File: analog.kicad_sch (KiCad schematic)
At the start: 51 parts, among them J10 Sensor harness, U8 ADS1115

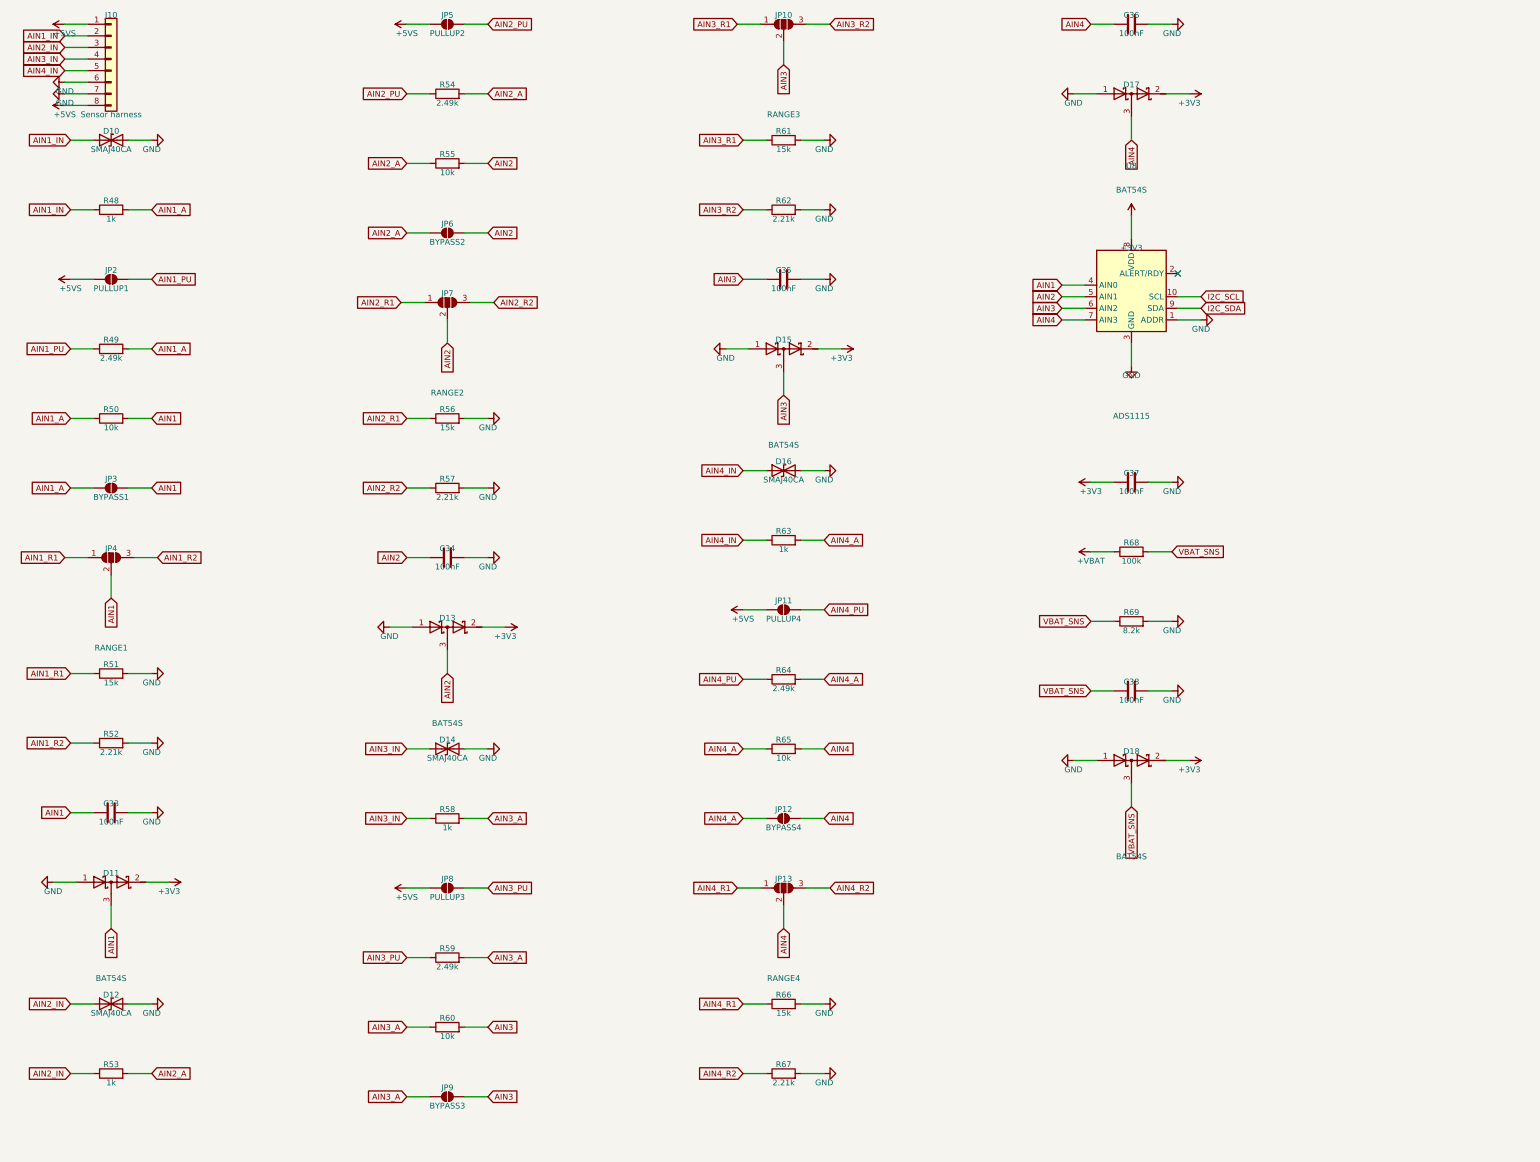
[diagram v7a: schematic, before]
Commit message: Rev B is fully routed: zero DRC errors, nothing unconnected
84 x 84 mm, 1447 tracks, 258 vias, 179 footprints, 106 nets.

The last few connections were never routing problems. Each one was a part
sited away from the net it belongs to, and the autorouter reporting "no
path at any width" was telling the truth:

  +5VS  the sensor rail's source (PF1/FB2/D3) sat on the right beside the
        WS2812 header while everything it feeds -- the sensor harness and
        all four channel pull-ups -- is on the left. The net existed as
        two complete halves with a 45 mm gap through buck islands and the
        SD socket. Moved the source to the harness side.
  IO46  the strapping pull-downs were parked in the bottom band while
        IO3/IO45/IO46 run from the module's south pads to J7 at the top
        left, so R29 needed a trace the length of the board to reach its
        own net. Moved them under the module's south pads.

Adding router passes had never touched either. Moving the parts fixed
both immediately -- worth remembering next time a net "cannot be routed".

Also in this pass:

  - One LED. D6 (amber) and D7 (blue) and their resistors are gone; D4
    green stays on +3V3, which is the right rail to watch because it only
    lights if the whole chain came through -- battery, ideal diode, both
    converters. That also retires review item 11.2.10, the blue emitter
    that would have been near-invisible on a 3.288 V rail.
  - J7 grows to six pins: the three strapping pins, the two GPIOs freed
    by the LEDs (IO15/IO16), and a ground pin. The missing ground was
    review item 13.4.13.
  - USB_CC1 gets a Fine netclass at 0.2 mm. There is no route at 0.25 mm
    -- the USB-C pads are on 0.5 mm pitch and will not pass it -- and CC
    carries under a milliamp through a 5.1k pull-down.
  - build_board.py takes a lock. Two builds sharing the board file is how
    one run died at "Specctra session import failed" after ten minutes,
    when a second build regenerated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
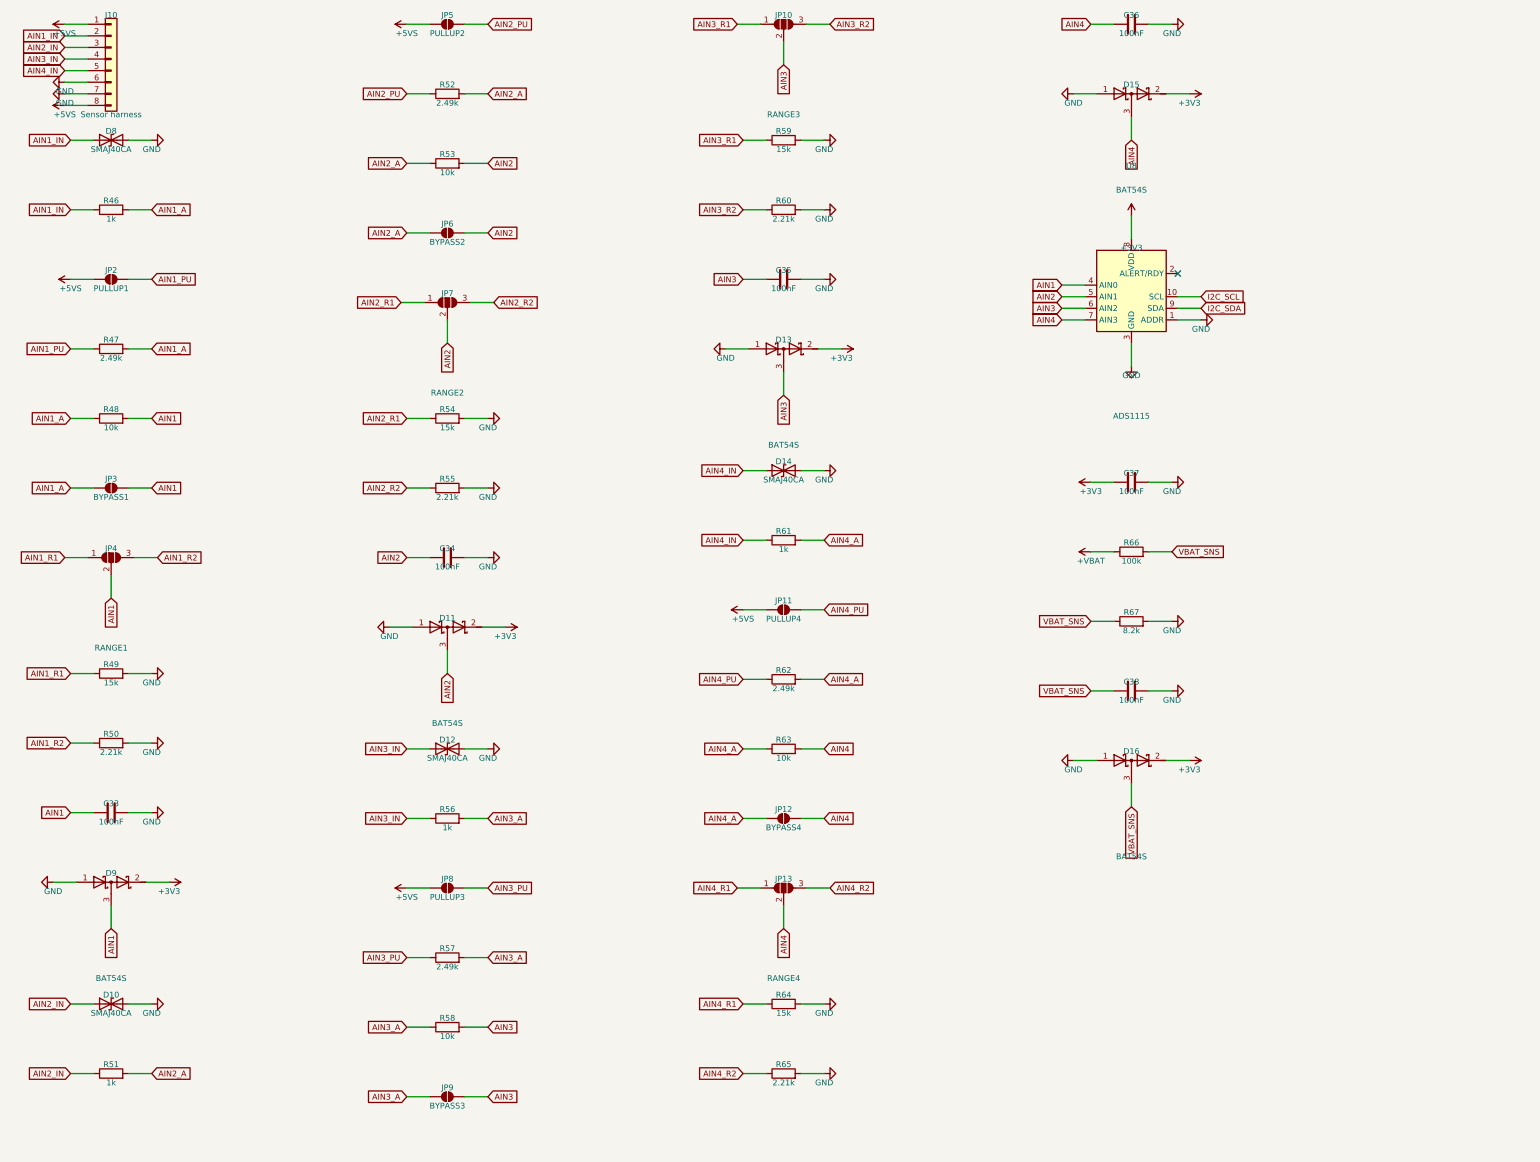
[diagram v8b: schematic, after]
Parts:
- removed D17, D18: BAT54S, Package_TO_SOT_SMD:SOT-23, symbol Device:D_Schottky_Dual_Series_AKC
- removed R68: 100k, Resistor_SMD:R_0805_2012Metric, symbol Device:R
- removed R69: 8.2k, Resistor_SMD:R_0805_2012Metric, symbol Device:R
- added D8: SMAJ40CA, Diode_SMD:D_SMA, symbol Device:D_TVS
- added D9: BAT54S, Package_TO_SOT_SMD:SOT-23, symbol Device:D_Schottky_Dual_Series_AKC
- added R46: 1k, Resistor_SMD:R_0805_2012Metric, symbol Device:R
- added R47: 2.49k, Resistor_SMD:R_0805_2012Metric, symbol Device:R
- D10: Note Ch1 harness transient clamp (bidirectional, 400W) -> Ch2 harness transient clamp (bidirectional, 400W)
- D11: Note Ch1 rail clamp (both polarities) -> Ch2 rail clamp (both polarities)
- D12: Note Ch2 harness transient clamp (bidirectional, 400W) -> Ch3 harness transient clamp (bidirectional, 400W)
- D13: Note Ch2 rail clamp (both polarities) -> Ch3 rail clamp (both polarities)
- D14: Note Ch3 harness transient clamp (bidirectional, 400W) -> Ch4 harness transient clamp (bidirectional, 400W)
- D15: Note Ch3 rail clamp (both polarities) -> Ch4 rail clamp (both polarities)
- D16: value SMAJ40CA -> BAT54S; footprint Diode_SMD:D_SMA -> Package_TO_SOT_SMD:SOT-23; symbol Device:D_TVS -> Device:D_Schottky_Dual_Series_AKC; MPN Littelfuse SMAJ40CA -> BAT54S; Note Ch4 harness transient clamp (bidirectional, 400W) -> Battery-monitor clamp
- R48: value 1k -> 10k; Note Ch1 series/fault-current limit; 0.1% thin film -- it is ins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 -> Ch1 divider upper leg, 0.1% thin film for AFR-grade accuracy
- R49: value 2.49k -> 15k; Note Ch1 bias resistor -> 0-5V range: 5.0V in -> ~2.88V at the ADC (1k series include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; Tolerance (none) -> 0.1%
- R50: value 10k -> 2.21k; Note Ch1 divider upper leg, 0.1% thin film for AFR-grade accuracy -> 0-16V range: 16.0V in -> ~2.67V at the ADC (1k series inclu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
- R51: value 15k -> 1k; Note 0-5V range: 5.0V in -> ~2.88V at the ADC (1k series include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 -> Ch2 series/fault-current limit; 0.1% thin film -- it is ins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
- R52: value 2.21k -> 2.49k; Note 0-16V range: 16.0V in -> ~2.67V at the ADC (1k series inclu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 -> Ch2 bias resistor; Tolerance 0.1% -> (none)
- R53: value 1k -> 10k; Note Ch2 series/fault-current limit; 0.1% thin film -- it is ins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 -> Ch2 divider upper leg, 0.1% thin film for AFR-grade accuracy
- R54: value 2.49k -> 15k; Note Ch2 bias resistor -> 0-5V range: 5.0V in -> ~2.88V at the ADC (1k series include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; Tolerance (none) -> 0.1%
- R55: value 10k -> 2.21k; Note Ch2 divider upper leg, 0.1% thin film for AFR-grade accuracy -> 0-16V range: 16.0V in -> ~2.67V at the ADC (1k series inclu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
- R56: value 15k -> 1k; Note 0-5V range: 5.0V in -> ~2.88V at the ADC (1k series include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 -> Ch3 series/fault-current limit; 0.1% thin film -- it is ins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
- R57: value 2.21k -> 2.49k; Note 0-16V range: 16.0V in -> ~2.67V at the ADC (1k series inclu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 -> Ch3 bias resistor; Tolerance 0.1% -> (none)
- R58: value 1k -> 10k; Note Ch3 series/fault-current limit; 0.1% thin film -- it is ins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 -> Ch3 divider upper leg, 0.1% thin film for AFR-grade accuracy
- R59: value 2.49k -> 15k; Note Ch3 bias resistor -> 0-5V range: 5.0V in -> ~2.88V at the ADC (1k series include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; Tolerance (none) -> 0.1%
- R60: value 10k -> 2.21k; Note Ch3 divider upper leg, 0.1% thin film for AFR-grade accuracy -> 0-16V range: 16.0V in -> ~2.67V at the ADC (1k series inclu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
- R61: value 15k -> 1k; Note 0-5V range: 5.0V in -> ~2.88V at the ADC (1k series include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 -> Ch4 series/fault-current limit; 0.1% thin film -- it is ins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
- R62: value 2.21k -> 2.49k; Note 0-16V range: 16.0V in -> ~2.67V at the ADC (1k series inclu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 -> Ch4 bias resistor; Tolerance 0.1% -> (none)
- R63: value 1k -> 10k; Note Ch4 series/fault-current limit; 0.1% thin film -- it is ins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 -> Ch4 divider upper leg, 0.1% thin film for AFR-grade accuracy
- R64: value 2.49k -> 15k; Note Ch4 bias resistor -> 0-5V range: 5.0V in -> ~2.88V at the ADC (1k series include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; Tolerance (none) -> 0.1%
- R65: value 10k -> 2.21k; Note Ch4 divider upper leg, 0.1% thin film for AFR-grade accuracy -> 0-16V range: 16.0V in -> ~2.67V at the ADC (1k series inclu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
- R66: value 15k -> 100k; Note 0-5V range: 5.0V in -> ~2.88V at the ADC (1k series include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 -> Battery monitor: divide by 11; Tolerance 0.1% -> (none)
- R67: value 2.21k -> 8.2k; Note 0-16V range: 16.0V in -> ~2.67V at the ADC (1k series inclu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 -> Divide by 13.2, not 11: at 36V the 11:1 divider put 3.27V o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; Tolerance 0.1% -> (none)
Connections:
- net +3V3: now also D16.2 (K), D9.2 (K)
- net +VBAT: now also R66.1
- net AIN1: now also R48.2, D9.3 (common); no longer D11.3 (common), R50.2
- net AIN1_A: now also R48.1, R46.2, R47.2; no longer R48.2, R49.2, R50.1
- net AIN1_IN: now also D8.1 (A1), R46.1; no longer D10.1 (A1), R48.1
- net AIN1_PU: now also R47.1; no longer R49.1
- net AIN1_R1: now also R49.1; no longer R51.1
- net AIN1_R2: now also R50.1; no longer R52.1
- net AIN2: now also D11.3 (common), R53.2; no longer D13.3 (common), R55.2
- net AIN2_A: now also R51.2, R52.2, R53.1; no longer R53.2, R54.2, R55.1
- net AIN2_IN: now also D10.1 (A1), R51.1; no longer D12.1 (A1), R53.1
- net AIN2_PU: now also R52.1; no longer R54.1
- net AIN2_R1: now also R54.1; no longer R56.1
- net AIN2_R2: now also R55.1; no longer R57.1
- net AIN3: now also D13.3 (common), R58.2; no longer D15.3 (common), R60.2
- net AIN3_A: now also R56.2, R57.2, R58.1; no longer R58.2, R59.2, R60.1
- net AIN3_IN: now also D12.1 (A1), R56.1; no longer D14.1 (A1), R58.1
- net AIN3_PU: now also R57.1; no longer R59.1
- net AIN3_R1: now also R59.1; no longer R61.1
- net AIN3_R2: now also R60.1; no longer R62.1
- net AIN4: now also D15.3 (common), R63.2; no longer R65.2
- net AIN4_A: now also R61.2, R62.2, R63.1; no longer R63.2, R64.2, R65.1
- net AIN4_IN: now also D14.1 (A1), R61.1; no longer D16.1 (A1), R63.1
- net AIN4_PU: now also R62.1; no longer R64.1
- net AIN4_R1: now also R64.1; no longer R66.1
- net AIN4_R2: now also R65.1; no longer R67.1
- net GND: now also D16.1 (A), R49.2, R50.2, R54.2, R55.2, R59.2, R60.2, R64.2, R65.2, D8.2 (A2), D9.1 (A); no longer D16.2 (A2), R51.2, R52.2, R56.2, R57.2, R61.2, R62.2, R66.2
- net VBAT_SNS: now also D16.3 (common), R66.2, R67.1
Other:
- moved on the sheet: D10, D11, D12, D13, D14, D15, R48, R49, R50, R51, R52, R53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
